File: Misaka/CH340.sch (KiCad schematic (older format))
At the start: 4 parts

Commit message: CH340C
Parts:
- added C12: 100nF, Capacitor_SMD:C_0603_1608Metric, symbol Device:C
- added C13: 22pF, Capacitor_SMD:C_0603_1608Metric, symbol Device:C
- added D1: CD1206, Diode_SMD:D_1206_3216Metric_Pad1.42x1.75mm_HandSolder, symbol Device:D
- added R22, R24, R25: 1k, Resistor_SMD:R_0603_1608Metric_Pad1.05x0.95mm_HandSolder, symbol Device:R
- added R23: 10k, Resistor_SMD:R_0603_1608Metric_Pad1.05x0.95mm_HandSolder, symbol Device:R
- added S1: MOMENTARY-SWITCH-SPST-PTH-6.0MM, TACTILE_SWITCH_PTH_6.0MM, symbol SparkFun-Switches:MOMENTARY-SWITCH-SPST-PTH-6.0MM
- C10, C11: renamed from C?; value C -> 100nF; footprint Capacitors:0603 -> Capacitor_SMD:C_0603_1608Metric
- gave numbers to parts that had none: 2
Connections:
- net +5V: now also D1.1 (K), R23.2; no longer J5.1 (VBUS)
- net GND: now also C13.1, R22.2, S1.3 (2)
- net RX: now also R25.1; no longer U5.3 (RXD)
- net TX: now also R24.1; no longer U5.2 (TXD)
- net at U5.13 (~DTR): now also C12.2, R22.1
- new net: R24.2, U5.2 (TXD)
- new net: R25.2, U5.3 (RXD)
- new net RESET: C12.1, C13.2, D1.2 (A), R23.1, S1.1
- no-connect marks 10 -> 9
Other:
- moved on the sheet: J5

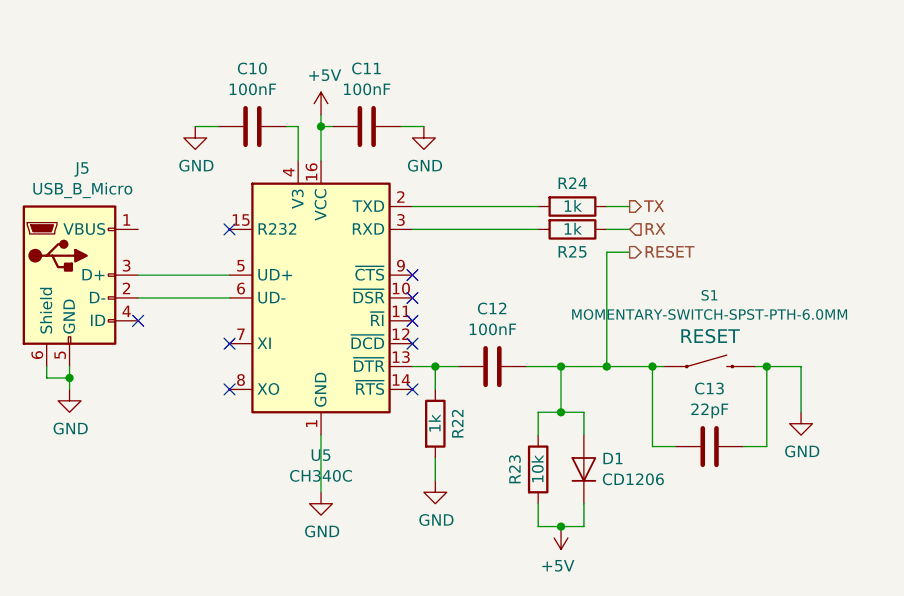
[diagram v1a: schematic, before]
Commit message: MURATA的 CSTLS16M0X51-A0
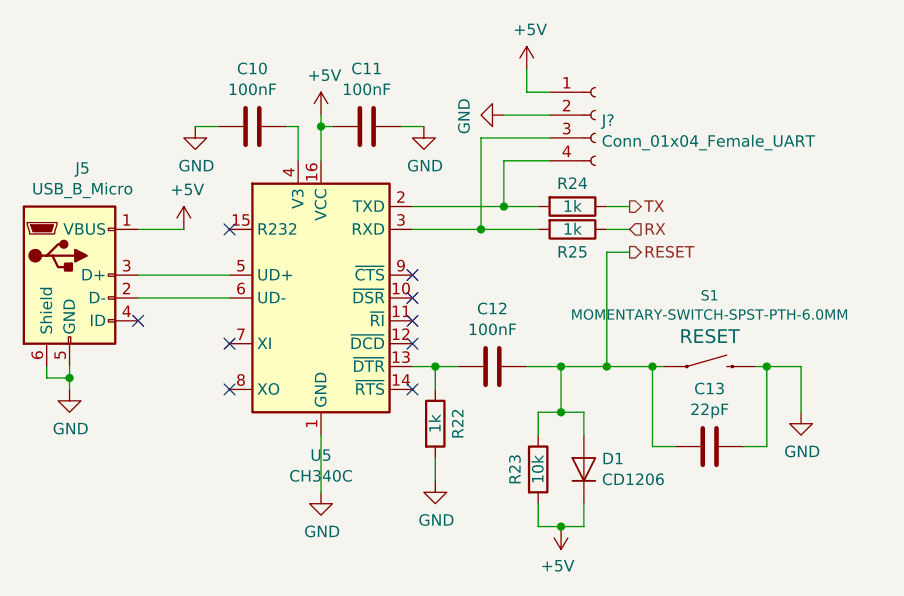
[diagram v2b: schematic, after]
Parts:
- added J?: Conn_01x04_Female_UART, Connector_PinSocket_2.54mm:PinSocket_1x04_P2.54mm_Vertical, symbol Connector:Conn_01x04_Female
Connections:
- net +5V: now also J5.1 (VBUS), J?.1 (Pin_1)
- net GND: now also J?.2 (Pin_2)
- net at R24.2, U5.2 (TXD): now also J?.4 (Pin_4)
- net at R25.2, U5.3 (RXD): now also J?.3 (Pin_3)
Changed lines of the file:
@@
 $Descr A4 11693 8268
 encoding utf-8
-Sheet 5 5
+Sheet 7 7
 Title ""
 Date ""
@@
 RESET
 Wire Wire Line
-	4550 1850 5100 1850
-Wire Wire Line
-	4550 1950 5100 1950
+	4550 1850 4950 1850
+Wire Wire Line
+	4550 1950 4850 1950
 Wire Wire Line
 	5500 2050 5400 2050
@@
 Wire Wire Line
 	3350 2250 3750 2250
+$Comp
+L Connector:Conn_01x04_Female J?
+U 1 1 5E60C088
+P 5350 1450
+F 0 "J?" H 5378 1426 50  0000 L CNN
+F 1 "Conn_01x04_Female_UART" H 5378 1335 50  0000 L CNN
+F 2 "Connector_PinSocket_2.54mm:PinSocket_1x04_P2.54mm_Vertical" H 5350 1450 50  0001 C CNN
+F 3 "~" H 5350 1450 50  0001 C CNN
+	1    5350 1450
+	1    0    0    -1
+$EndComp
+Wire Wire Line
+	4950 1850 4950 1650
+Wire Wire Line
+	4950 1650 5150 1650
+Connection ~ 4950 1850
+Wire Wire Line
+	4950 1850 5100 1850
+Wire Wire Line
+	4850 1950 4850 1550
+Wire Wire Line
+	4850 1550 5150 1550
+Connection ~ 4850 1950
+Wire Wire Line
+	4850 1950 5100 1950
+$Comp
+L power:GND #PWR?
+U 1 1 5E6138D2
+P 4950 1450
+F 0 "#PWR?" H 4950 1200 50  0001 C CNN
+F 1 "GND" H 4955 1277 50  0000 C CNN
+F 2 "" H 4950 1450 50  0001 C CNN
+F 3 "" H 4950 1450 50  0001 C CNN
+	1    4950 1450
+	0    1    1    0
+$EndComp
+$Comp
+L power:+5V #PWR?
+U 1 1 5E614188
+P 5050 1250
+F 0 "#PWR?" H 5050 1100 50  0001 C CNN
+F 1 "+5V" H 5065 1423 50  0000 C CNN
+F 2 "" H 5050 1250 50  0001 C CNN
+F 3 "" H 5050 1250 50  0001 C CNN
+	1    5050 1250
+	1    0    0    -1
+$EndComp
+Wire Wire Line
+	4950 1450 5150 1450
+Wire Wire Line
+	5150 1350 5050 1350
+Wire Wire Line
+	5050 1350 5050 1250
+$Comp
+L power:+5V #PWR?
+U 1 1 5E64CBD9
+P 3550 1950
+F 0 "#PWR?" H 3550 1800 50  0001 C CNN
+F 1 "+5V" H 3565 2123 50  0000 C CNN
+F 2 "" H 3550 1950 50  0001 C CNN
+F 3 "" H 3550 1950 50  0001 C CNN
+	1    3550 1950
+	1    0    0    -1
+$EndComp
+Wire Wire Line
+	3350 1950 3550 1950
 $EndSCHEMATC

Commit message: V1
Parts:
- gave numbers to parts that had none: 1
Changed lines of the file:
@@
 $Descr A4 11693 8268
 encoding utf-8
-Sheet 7 7
+Sheet 7 10
 Title ""
 Date ""
@@
 	3350 2250 3750 2250
 $Comp
-L Connector:Conn_01x04_Female J?
+L Connector:Conn_01x04_Female J7
 U 1 1 5E60C088
 P 5350 1450
-F 0 "J?" H 5378 1426 50  0000 L CNN
+F 0 "J7" H 5378 1426 50  0000 L CNN
 F 1 "Conn_01x04_Female_UART" H 5378 1335 50  0000 L CNN
 F 2 "Connector_PinSocket_2.54mm:PinSocket_1x04_P2.54mm_Vertical" H 5350 1450 50  0001 C CNN
@@
 	4850 1950 5100 1950
 $Comp
-L power:GND #PWR?
+L power:GND #PWR0171
 U 1 1 5E6138D2
 P 4950 1450
-F 0 "#PWR?" H 4950 1200 50  0001 C CNN
+F 0 "#PWR0171" H 4950 1200 50  0001 C CNN
 F 1 "GND" H 4955 1277 50  0000 C CNN
 F 2 "" H 4950 1450 50  0001 C CNN
@@
 $EndComp
 $Comp
-L power:+5V #PWR?
+L power:+5V #PWR0172
 U 1 1 5E614188
 P 5050 1250
-F 0 "#PWR?" H 5050 1100 50  0001 C CNN
+F 0 "#PWR0172" H 5050 1100 50  0001 C CNN
 F 1 "+5V" H 5065 1423 50  0000 C CNN
 F 2 "" H 5050 1250 50  0001 C CNN
@@
 	5050 1350 5050 1250
 $Comp
-L power:+5V #PWR?
+L power:+5V #PWR0173
 U 1 1 5E64CBD9
 P 3550 1950
-F 0 "#PWR?" H 3550 1800 50  0001 C CNN
+F 0 "#PWR0173" H 3550 1800 50  0001 C CNN
 F 1 "+5V" H 3565 2123 50  0000 C CNN
 F 2 "" H 3550 1950 50  0001 C CNN

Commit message: route v2.1
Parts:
- C10, C11, C12, C13: footprint Capacitor_SMD:C_0603_1608Metric -> Capacitor_SMD:C_0603_1608Metric_Pad1.05x0.95mm_HandSolder
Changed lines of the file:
@@
 F 0 "C10" V 3598 1500 50  0000 C CNN
 F 1 "100nF" V 3689 1500 50  0000 C CNN
-F 2 "Capacitor_SMD:C_0603_1608Metric" H 3888 1350 50  0001 C CNN
+F 2 "Capacitor_SMD:C_0603_1608Metric_Pad1.05x0.95mm_HandSolder" H 3888 1350 50  0001 C CNN
 F 3 "~" H 3850 1500 50  0001 C CNN
 	1    3850 1500
@@
 F 0 "C11" V 4098 1500 50  0000 C CNN
 F 1 "100nF" V 4189 1500 50  0000 C CNN
-F 2 "Capacitor_SMD:C_0603_1608Metric" H 4388 1350 50  0001 C CNN
+F 2 "Capacitor_SMD:C_0603_1608Metric_Pad1.05x0.95mm_HandSolder" H 4388 1350 50  0001 C CNN
 F 3 "~" H 4350 1500 50  0001 C CNN
 	1    4350 1500
@@
 F 0 "C12" V 4648 2550 50  0000 C CNN
 F 1 "100nF" V 4739 2550 50  0000 C CNN
-F 2 "Capacitor_SMD:C_0603_1608Metric" H 4938 2400 50  0001 C CNN
+F 2 "Capacitor_SMD:C_0603_1608Metric_Pad1.05x0.95mm_HandSolder" H 4938 2400 50  0001 C CNN
 F 3 "~" H 4900 2550 50  0001 C CNN
 	1    4900 2550
@@
 F 0 "C13" V 5598 2900 50  0000 C CNN
 F 1 "22pF" V 5689 2900 50  0000 C CNN
-F 2 "Capacitor_SMD:C_0603_1608Metric" H 5888 2750 50  0001 C CNN
+F 2 "Capacitor_SMD:C_0603_1608Metric_Pad1.05x0.95mm_HandSolder" H 5888 2750 50  0001 C CNN
 F 3 "~" H 5850 2900 50  0001 C CNN
 	1    5850 2900

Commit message: Change Footprint
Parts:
- S1: value MOMENTARY-SWITCH-SPST-PTH-6.0MM -> TACTILE_SWITCH_SMD_4.5MM; footprint TACTILE_SWITCH_PTH_6.0MM -> Switches:TACTILE_SWITCH_SMD_4.5MM; symbol SparkFun-Switches:MOMENTARY-SWITCH-SPST-PTH-6.0MM -> Switch:SW_Push
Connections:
- net GND: now also S1.2; no longer S1.3 (2)
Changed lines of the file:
@@
 	4650 2950 4650 3050
 $Comp
-L SparkFun-Switches:MOMENTARY-SWITCH-SPST-PTH-6.0MM S1
+L Switch:SW_Push S1
 U 1 1 5E63B4DB
 P 5850 2550
 F 0 "S1" H 5850 2860 45  0000 C CNN
-F 1 "MOMENTARY-SWITCH-SPST-PTH-6.0MM" H 5850 2776 45  0000 C CNN
-F 2 "TACTILE_SWITCH_PTH_6.0MM" H 5850 2750 20  0001 C CNN
+F 1 "TACTILE_SWITCH_SMD_4.5MM" H 5850 2776 45  0000 C CNN
+F 2 "Switches:TACTILE_SWITCH_SMD_4.5MM" H 5850 2750 20  0001 C CNN
 F 3 "" H 5850 2550 50  0001 C CNN
 F 4 "RESET" H 5850 2681 60  0000 C CNN "Field4"

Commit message: route v2.2
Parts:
- S1: symbol Switch:SW_Push -> SparkFun-Switches:MOMENTARY-SWITCH-SPST-SMD-4.5MM
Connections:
- net GND: now also S1.1 (2), S1.4 (2); no longer S1.2
- net RESET: now also S1.2 (1), S1.3 (1); no longer S1.1
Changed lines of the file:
@@
 $Descr A4 11693 8268
 encoding utf-8
-Sheet 7 10
+Sheet 10 10
 Title ""
 Date ""
@@
 	4650 2950 4650 3050
 $Comp
-L Switch:SW_Push S1
+L SparkFun-Switches:MOMENTARY-SWITCH-SPST-SMD-4.5MM S1
 U 1 1 5E63B4DB
 P 5850 2550
